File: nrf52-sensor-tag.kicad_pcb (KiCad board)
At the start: 2 copper layers, 32.8 x 32.8 mm, 18 parts, among them IC1 ISP1807-LR-RS, IC2 MAX44009EDT+T, U1 BME280

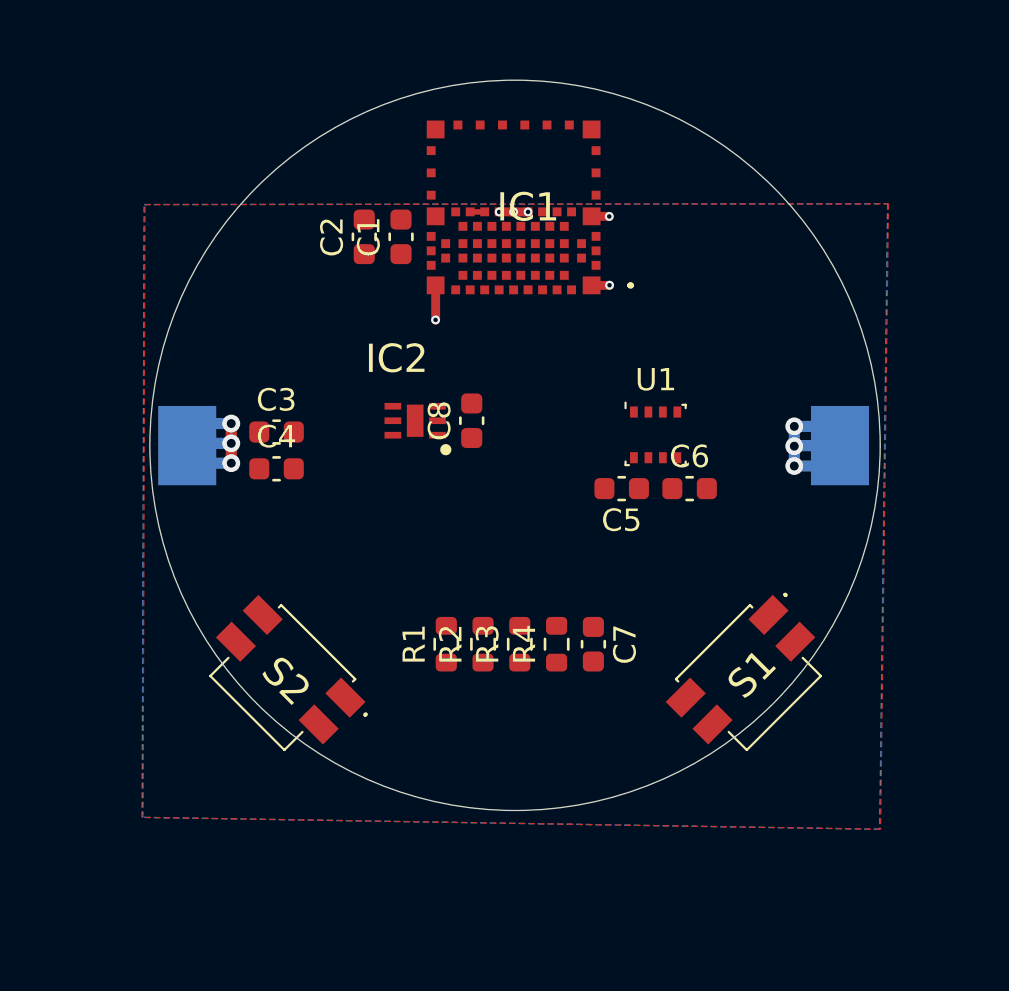
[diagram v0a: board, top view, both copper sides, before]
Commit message: Moved components and routed the board
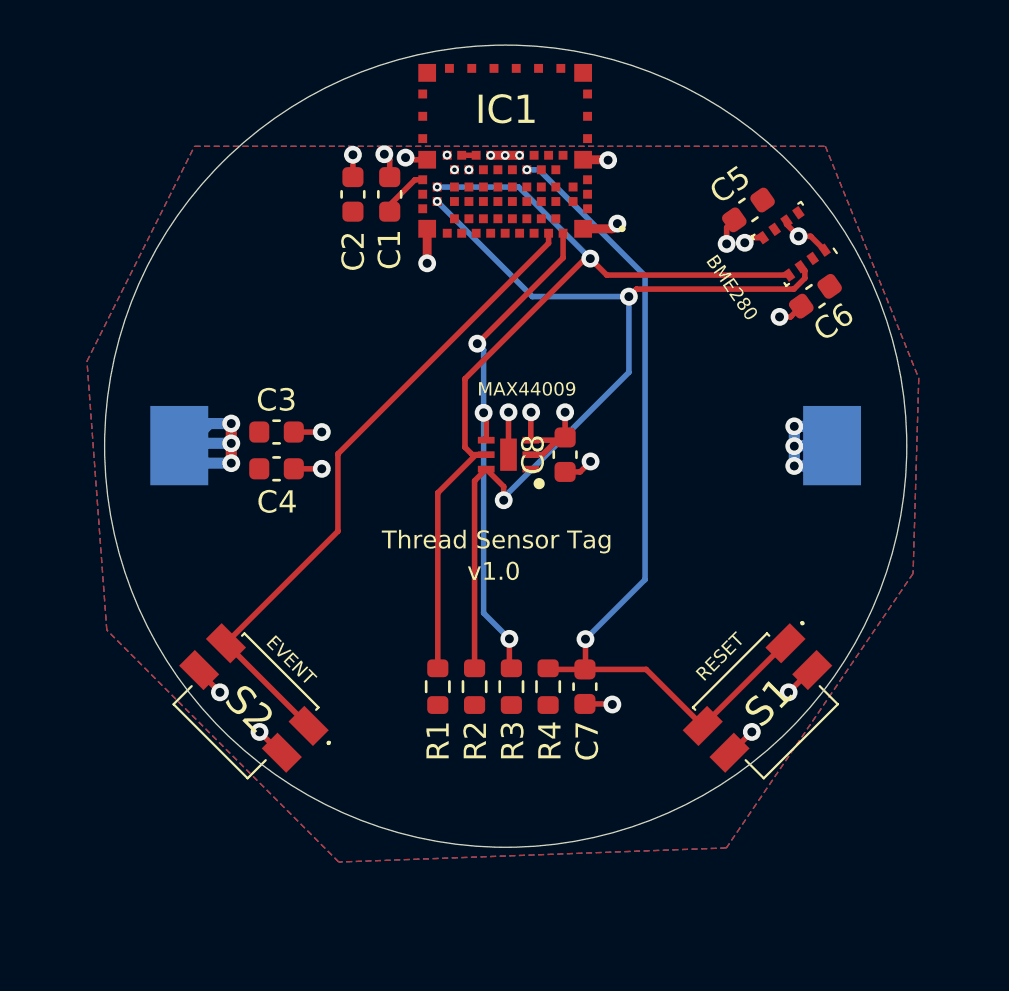
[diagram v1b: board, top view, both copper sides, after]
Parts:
- moved C5 13.7 mm to (132.7, 54.0), turned to 215 degrees
- moved U1 10.6 mm to (134.7, 55.6), turned to 215 degrees
- moved C6 10.3 mm to (135.7, 57.9), turned to 215 degrees
- moved C8 4.46 mm to (124.4, 65.0)
- moved IC2 4.46 mm to (121.9, 65.0)
- moved IC1 2.57 mm to (121.7, 51.4)
- moved S2 2.08 mm to (110.5, 75.9)
- moved C1 1.97 mm to (116.6, 53.3)
- moved C2 1.97 mm to (114.9, 53.3)
- moved C7 1.94 mm to (125.3, 75.4)
- moved R1 1.94 mm to (118.7, 75.4)
- moved R2 1.94 mm to (120.4, 75.4)
- moved R3 1.94 mm to (122.0, 75.4)
- moved R4 1.94 mm to (123.7, 75.4)
- moved S1 1.48 mm to (133.1, 75.9)
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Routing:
- net /SDA: track 0.00 -> 41.5 mm, vias 0 -> 3
- net /SCL: track 0.00 -> 40.2 mm, vias 0 -> 2
- net /RESET: track 0.00 -> 39.3 mm, vias 0 -> 2
- net /BTN: track 0.00 -> 29.7 mm
- net GND: track 13.1 -> 40.6 mm, vias 9 -> 29
- net /~INT1: track 0.00 -> 23.0 mm, vias 0 -> 3
- net /VCC: track 8.48 -> 12.1 mm, vias 3 -> 4
- added copper zone on F.Cu, net /VCC
- added copper zone on B.Cu, net GND
- removed copper zone on B.Cu, net (none)
- removed copper zone on F.Cu, net GND
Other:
- board size 32.8 x 32.8 mm -> 36 x 36 mm
- board text added: "BME280"
- board text added: "EVENT"
- board text added: "MAX44009"
- board text added: "RESET"
- board text added: "Thread Sensor Tag"
- board text added: "v1.0"

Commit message: Attached the sensors VCC to GPIOs of the nrf instead vcc (incl. a jumper just in case)
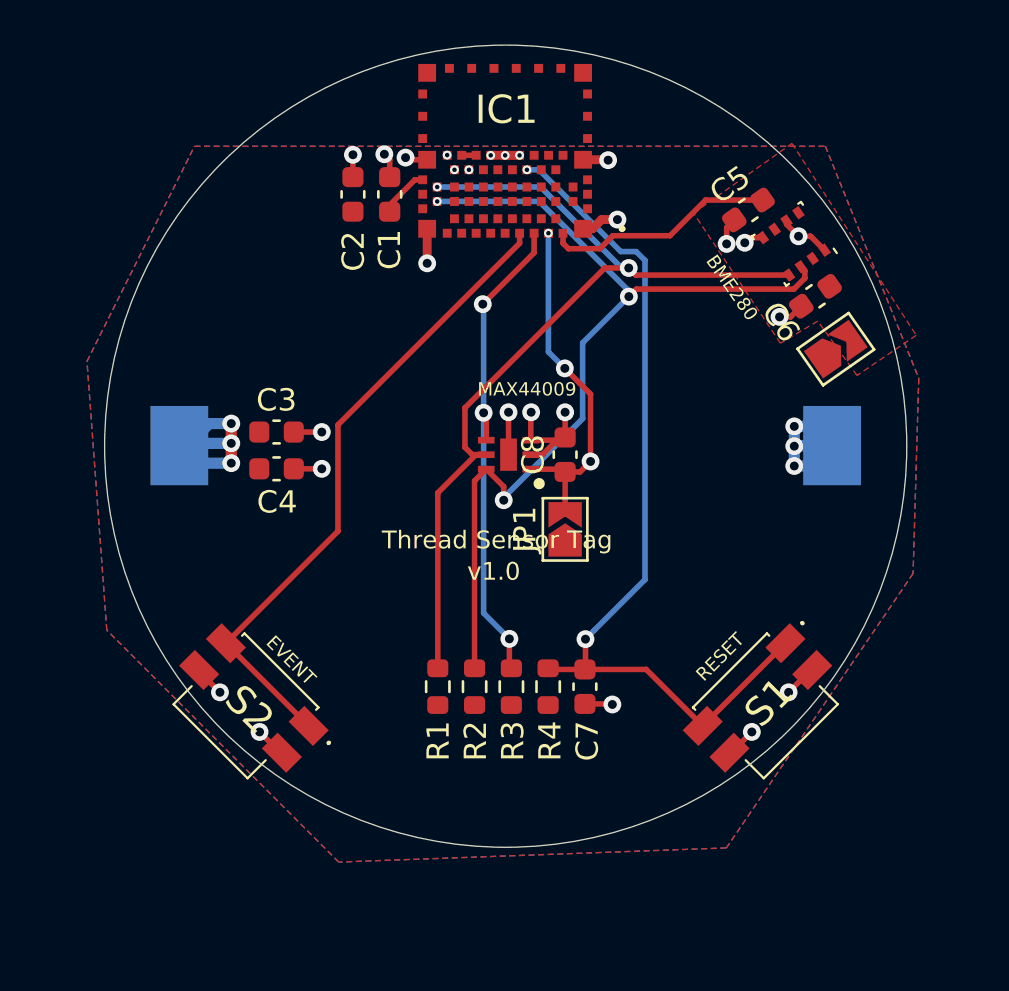
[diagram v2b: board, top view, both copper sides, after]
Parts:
- added JP1: Jumper_NC_Small, Jumper:SolderJumper-2_P1.3mm_Open_TrianglePad1.0x1.5mm, F.Cu at (124.4, 68.4)
- added JP2: Jumper_NC_Small, Jumper:SolderJumper-2_P1.3mm_Open_TrianglePad1.0x1.5mm, F.Cu at (136.6, 60.3)
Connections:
- C5 pad 1: /VCC -> /BME280_VCC
- C6 pad 1: /VCC -> /BME280_VCC
- C8 pad 1: /VCC -> /MAX44_VCC
- IC1 pad 42: Net-(IC1-Pad42) -> /BTN
- IC1 pad 44: Net-(IC1-Pad44) -> /~INT1
- IC1 pad 46: /BTN -> /MAX44_VCC
- IC1 pad 48: /~INT1 -> /BME280_VCC
- IC2 pad 1: /VCC -> /MAX44_VCC
- U1 pad 2: /VCC -> /BME280_VCC
- U1 pad 6: /VCC -> /BME280_VCC
- U1 pad 8: /VCC -> /BME280_VCC
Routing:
- net /MAX44_VCC: track 0.00 -> 15.8 mm, vias 0 -> 3
- net /BME280_VCC: track 0.00 -> 10.4 mm
- net /VCC: track 12.1 -> 10.7 mm, vias 4 -> 3
- net /SCL: track 40.2 -> 41.0 mm
- net /~INT1: track 23.0 -> 22.3 mm
- net /BTN: track 29.7 -> 29.1 mm
- added copper zone on F.Cu, net /BME280_VCC

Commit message: Add debug connector
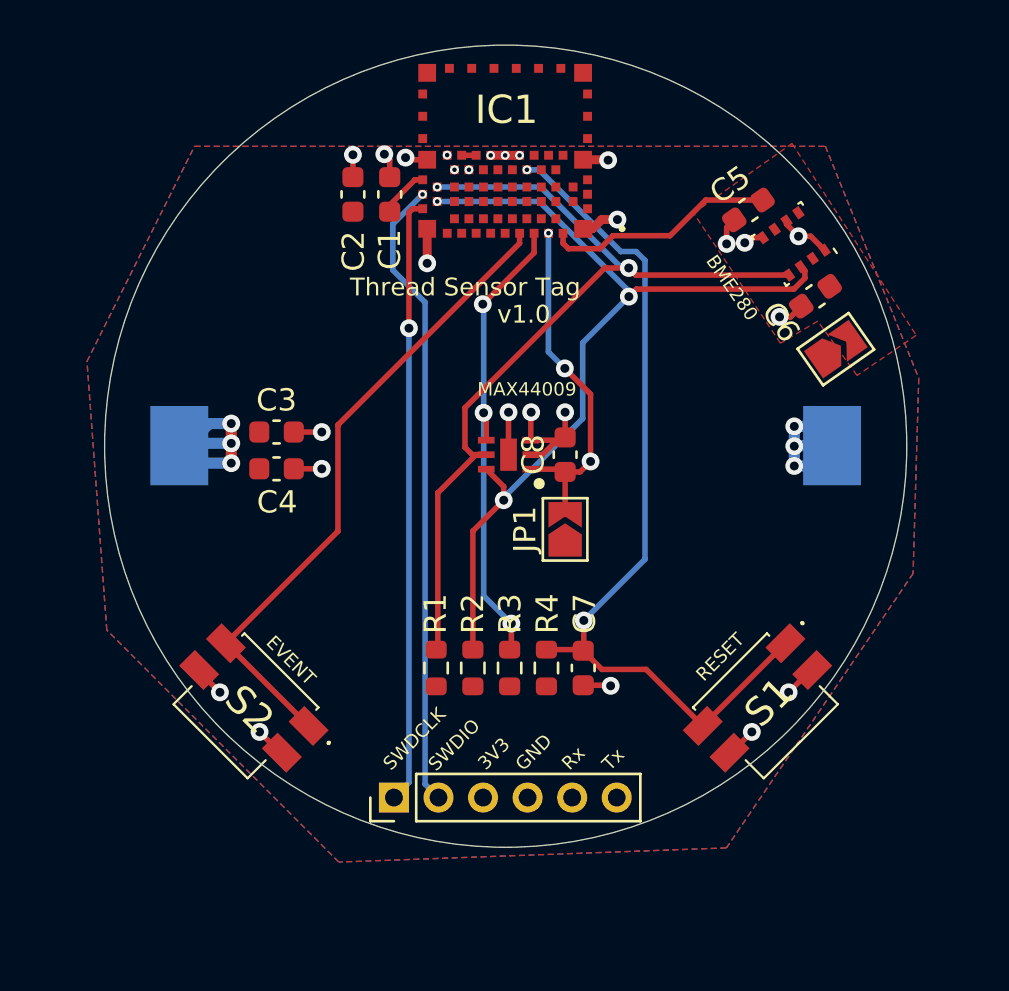
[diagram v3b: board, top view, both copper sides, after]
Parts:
- added J1: Conn_01x06_Male, Connector_PinHeader_2.00mm:PinHeader_1x06_P2.00mm_Vertical, F.Cu at (116.8, 80.4)
- moved C7 0.84 mm to (125.2, 74.6)
- moved R1 0.84 mm to (118.6, 74.6)
- moved R2 0.84 mm to (120.3, 74.6)
- moved R3 0.84 mm to (121.9, 74.6)
- moved R4 0.84 mm to (123.6, 74.6)
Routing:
- net /SWDIO: track 0.00 -> 28.5 mm, vias 0 -> 1
- net /SWDCLK: track 0.00 -> 27.2 mm, vias 0 -> 1
- net /SDA: track 41.7 -> 39.8 mm
- net /~INT1: track 22.3 -> 21.5 mm
- net /SCL: track 41.0 -> 40.2 mm
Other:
- board text added: "3V3"
- board text added: "GND"
- board text added: "Rx"
- board text added: "SWDCLK"
- board text added: "SWDIO"
- board text added: "Tx"

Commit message: Beautify schematics + added debug connector
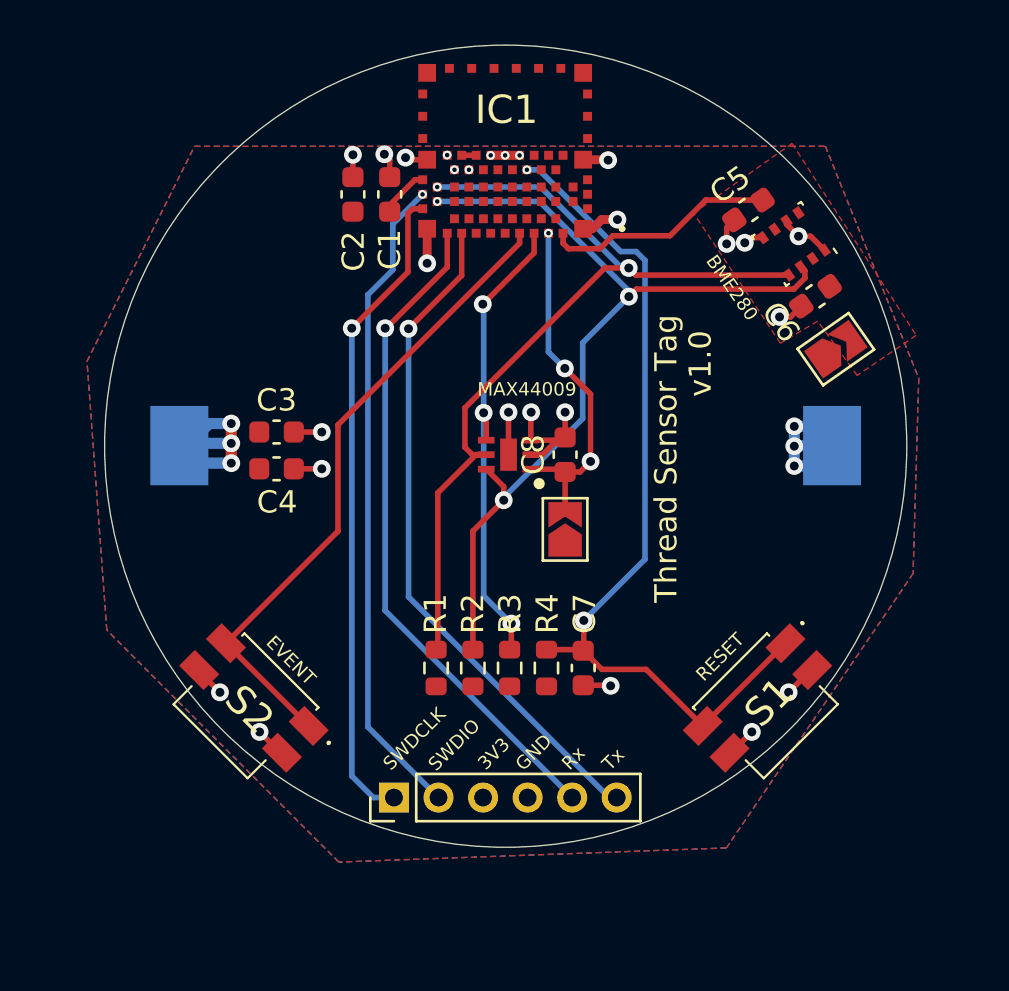
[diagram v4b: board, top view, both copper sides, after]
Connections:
- IC1 pad 32: Net-(IC1-Pad32) -> /Rx
- IC1 pad 34: Net-(IC1-Pad34) -> /Tx
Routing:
- net /Tx: track 0.00 -> 30.4 mm, vias 0 -> 1
- net /Rx: track 0.00 -> 30.0 mm, vias 0 -> 1
- net /SWDCLK: track 27.2 -> 29.3 mm
- net /SWDIO: track 28.5 -> 29.4 mm

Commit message: Finalized layout
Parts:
- removed J1: Conn_01x06_Male, Connector_PinHeader_2.00mm:PinHeader_1x06_P2.00mm_Vertical
- added J3: Conn_01x07_Male, Connector_PinHeader_2.54mm:PinHeader_1x07_P2.54mm_Vertical, F.Cu at (114.1, 78.9)
- moved R3 11.3 mm to (115.7, 65.2)
- moved R2 9.89 mm to (117.4, 65.2), turned to 270 degrees
- moved R1 9.45 mm to (119.0, 65.2), turned to 270 degrees
- moved R4 6.14 mm to (129.5, 72.9)
- moved C7 6.14 mm to (131.1, 72.9)
- moved S2 4.17 mm to (107.9, 72.6), turned to 120 degrees
- moved S1 4.17 mm to (135.6, 72.6), turned to 60 degrees
- moved JP1 0.06 mm to (124.4, 68.3)
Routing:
- net /SCL: track 40.2 -> 33.1 mm
- net /RESET: track 39.3 -> 35.1 mm
- net /Tx: track 30.4 -> 33.7 mm
- net /~INT1: track 21.5 -> 18.5 mm, vias 3 -> 2
- net /SDA: track 39.8 -> 37.2 mm
- net /SWDCLK: track 29.3 -> 26.7 mm
- net /Rx: track 30.0 -> 32.4 mm
- net /SWDIO: track 29.4 -> 27.0 mm
- net /BTN: track 29.1 -> 30.4 mm, vias 0 -> 2
- net GND: track 40.6 -> 41.7 mm
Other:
- board text added: "DEBUG"
- board text added: "UART"

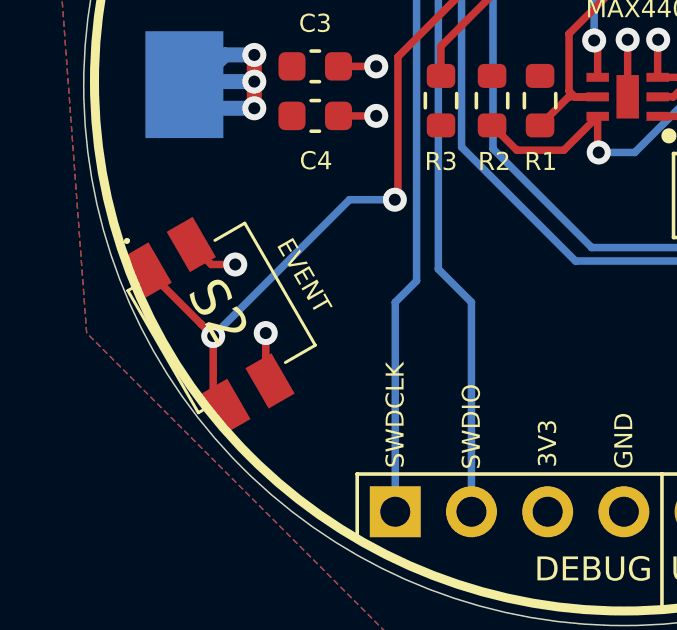
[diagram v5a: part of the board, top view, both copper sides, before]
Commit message: Fix button orientation
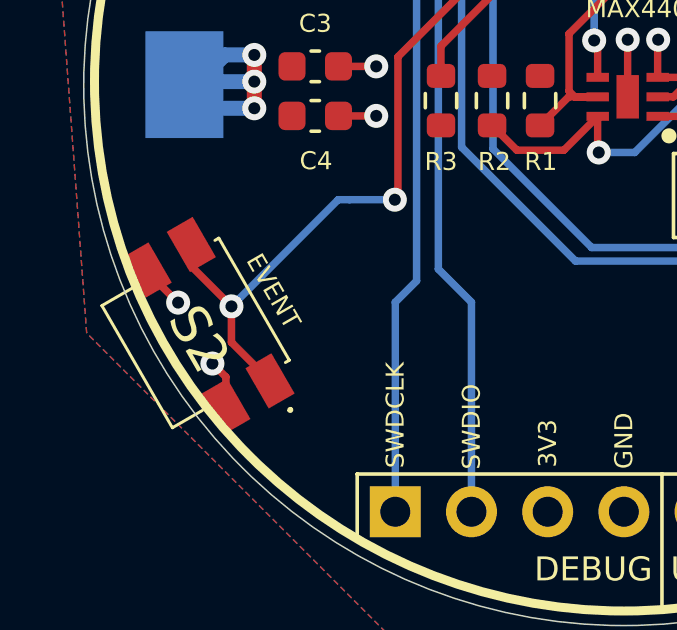
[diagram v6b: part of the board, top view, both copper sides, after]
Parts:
- turned S2 to 300 degrees
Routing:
- net /BTN: track 30.4 -> 29.6 mm

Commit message: Add new alternative sensors
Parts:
- removed U1: BME280, Package_LGA:Bosch_LGA-8_2.5x2.5mm_P0.65mm_ClockwisePinNumbering
- added IC3: MS860702BA01-50, MS860702BA01-50:SON125P300X500X100-8N, F.Cu at (133.4, 56.3)
- added R5: 10R, Resistor_SMD:R_0603_1608Metric, F.Cu at (125.5, 64.3)
- C5: value 0.1uF -> 0.22uF
- C6: value 0.1uF -> 10uF
- C8: value 1uF -> 0.1uF
- IC2: value MAX44009EDT+T -> VEML6030; footprint MAX44009EDT+T:SON65P200X200X65-7N-D -> VEML6030:VEML6030
- R1, R2: value 10k -> 4.7k
- moved C6 9.58 mm to (128.5, 64.3), turned to 270 degrees
- moved C8 2.65 mm to (127.0, 64.3), turned to 270 degrees
- moved R3 2.33 mm to (117.7, 64.0), turned to 270 degrees
- moved C5 1.91 mm to (130.8, 53.7), turned to 35 degrees
- moved R2 1.75 mm to (116.1, 64.0)
- moved R1 1.20 mm to (119.4, 64.0)
- moved IC2 1.02 mm to (122.4, 64.1), turned to 0 degrees
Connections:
- C5 pad 1: /BME280_VCC -> /SENS1_VCC
- C6 pad 1: /BME280_VCC -> /SENS2_VCC
- C8 pad 1: /MAX44_VCC -> /SENS2_VCC
- IC1 pad 46: /MAX44_VCC -> /SENS2_VCC
- IC1 pad 48: /BME280_VCC -> /SENS1_VCC
- IC2 pad 1: /MAX44_VCC -> GND
- IC2 pad 2: GND -> /SDA
- IC2 pad 3: GND -> /INT1
- IC2 pad 4: /~INT1 -> Net-(IC2-Pad4)
- IC2 pad 6: /SDA -> Net-(IC2-Pad4)
- JP1 pad 2: /MAX44_VCC -> /SENS2_VCC
- JP2 pad 2: /BME280_VCC -> /SENS1_VCC
- R3 pad 2: /~INT1 -> /INT1
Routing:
- net /SENS2_VCC: track 0.00 -> 21.0 mm, vias 0 -> 2
- net /~INT1: track 18.5 -> 0.00 mm, vias 2 -> 0
- net /MAX44_VCC: track 15.8 -> 0.00 mm, vias 3 -> 0
- net /BME280_VCC: track 10.4 -> 0.00 mm
- net GND: track 41.9 -> 34.2 mm, vias 29 -> 27
- net /SENS1_VCC: track 0.00 -> 6.96 mm
- net /INT1: track 0.00 -> 4.63 mm
- net Net-(IC2-Pad4): track 0.00 -> 4.61 mm
- net /SDA: track 37.2 -> 39.3 mm
- net /SCL: track 33.1 -> 33.9 mm
- added copper zone on F.Cu, net /SENS1_VCC
- removed copper zone on F.Cu, net /BME280_VCC
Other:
- board text added: "MS8607"
- board text added: "VEML6030"
- board text removed: "BME280"
- board text removed: "MAX44009"
